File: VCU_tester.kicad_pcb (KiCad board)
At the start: 2 copper layers, 54.6 x 86.4 mm, 2 parts, among them P8 BeagleBone_Black_Header, P9 BeagleBone_Black_Header

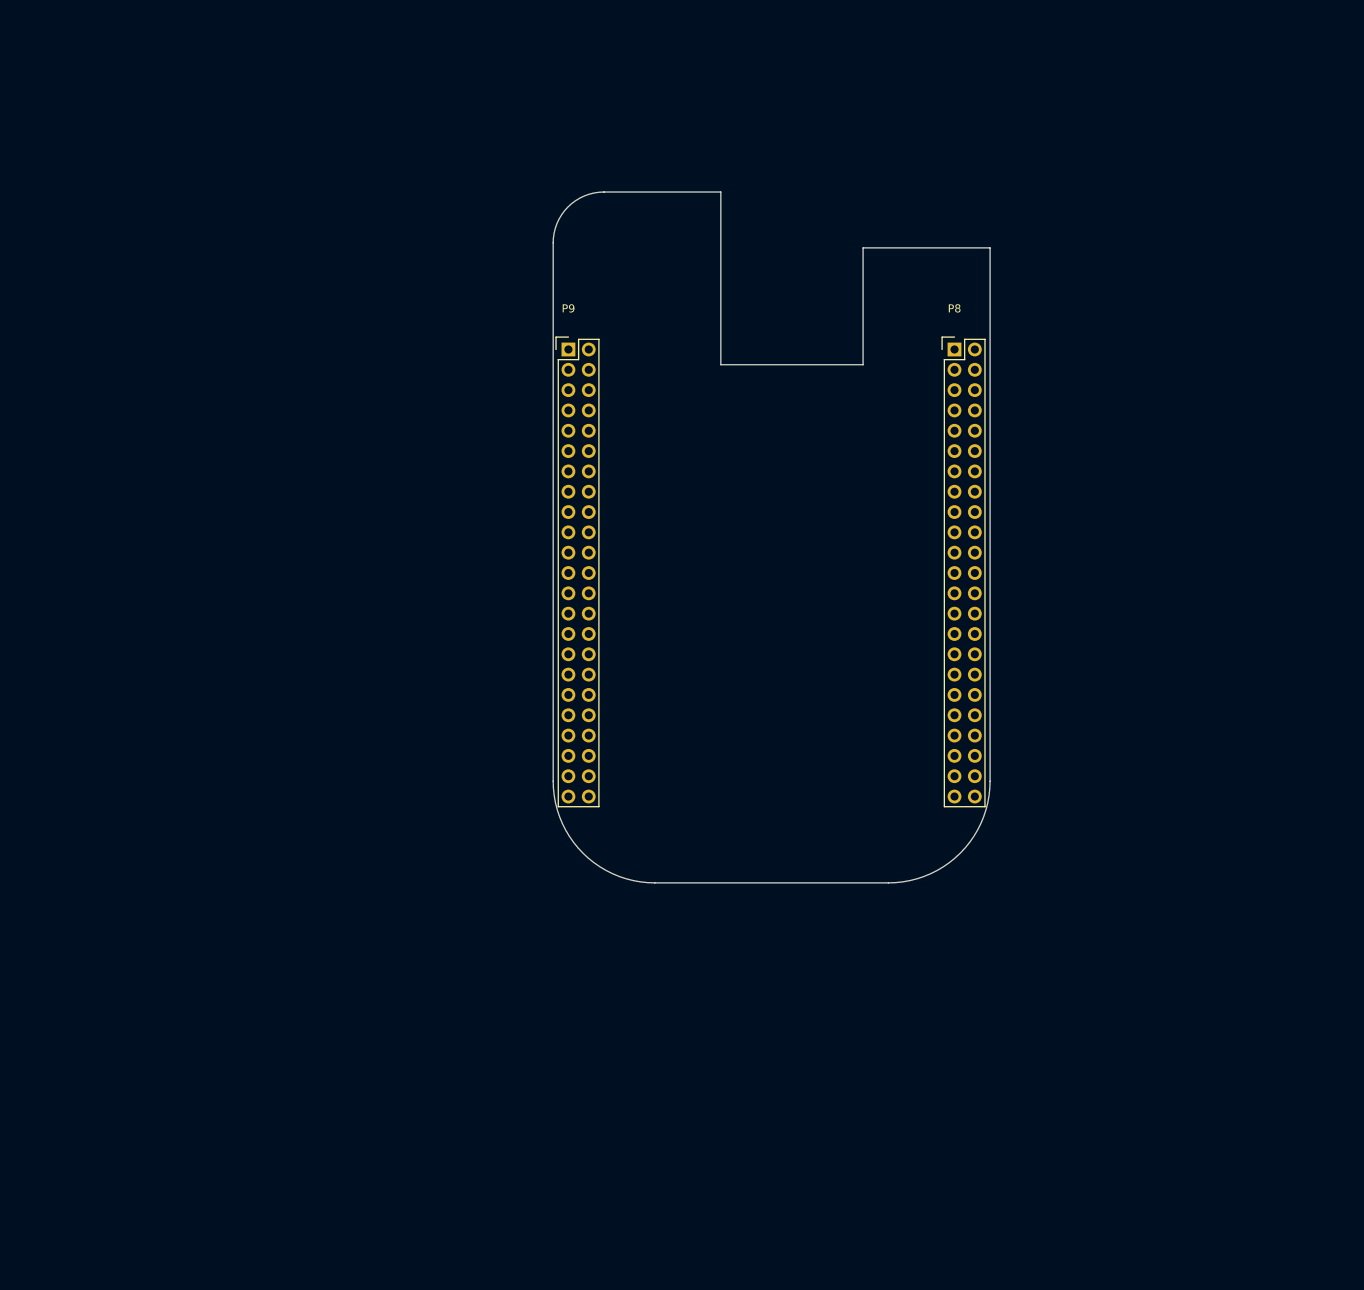
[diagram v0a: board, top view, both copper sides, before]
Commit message: parts assigned, layout started, CAN and RS232 sides done
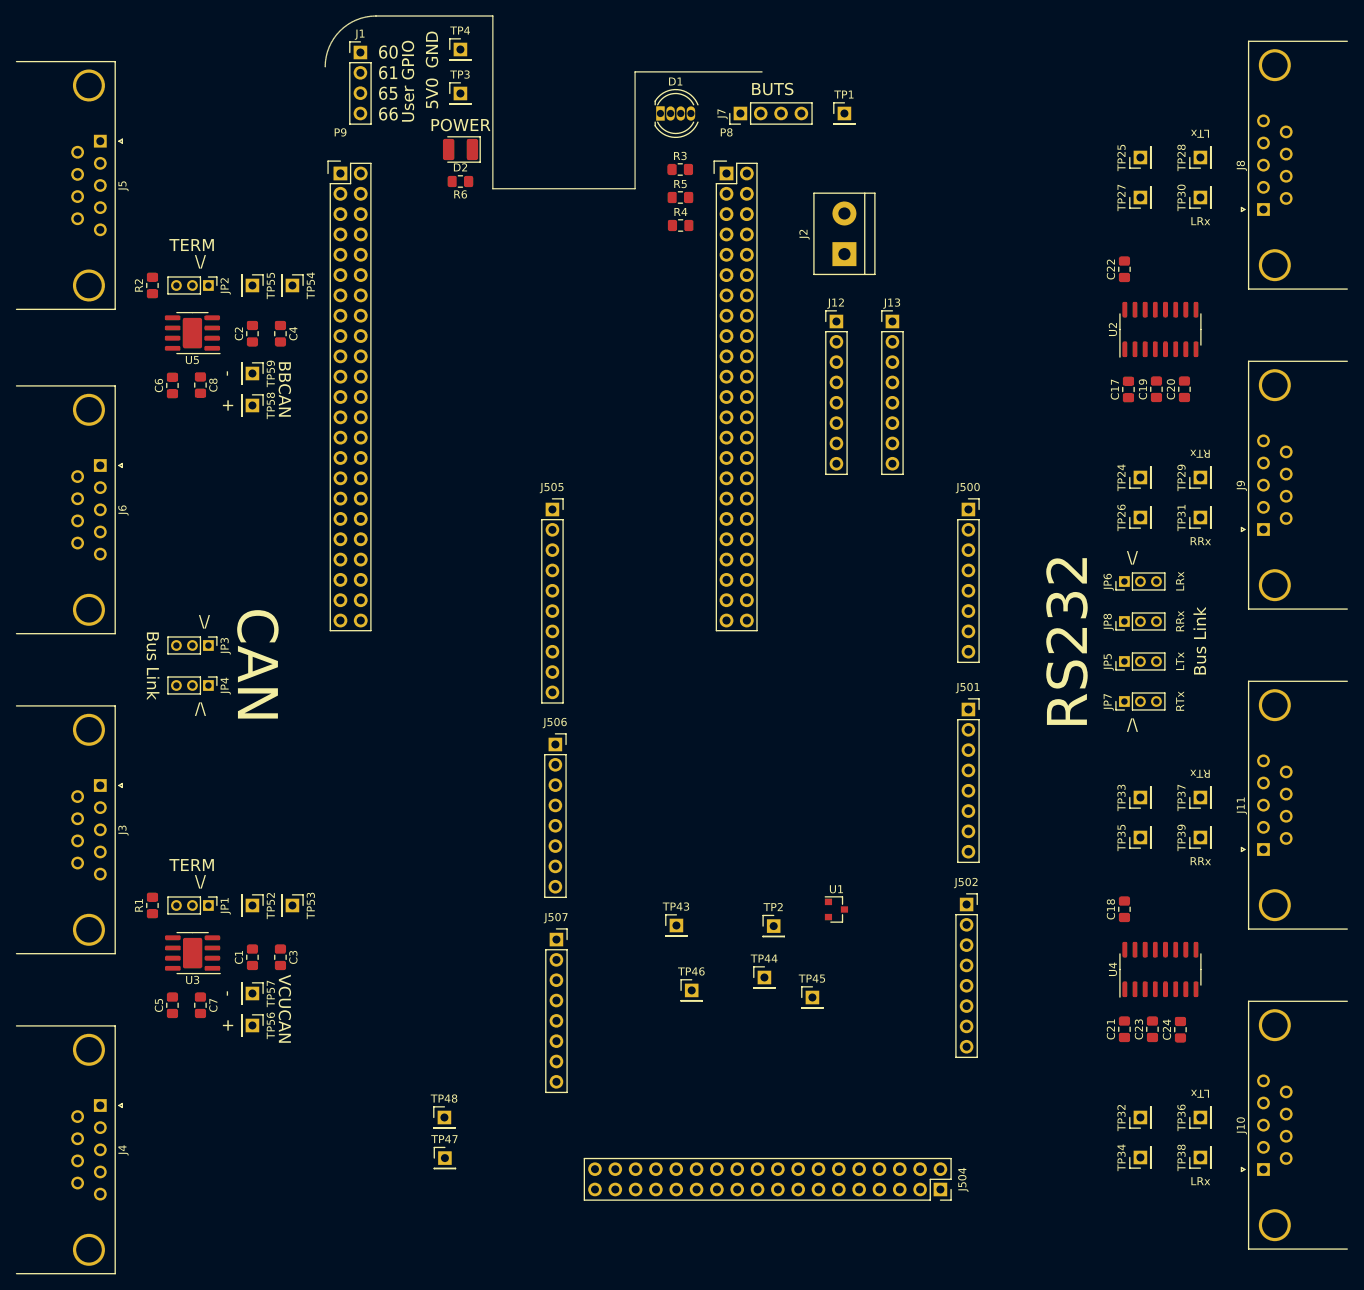
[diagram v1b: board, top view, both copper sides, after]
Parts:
- added C1: 10u, Capacitor_SMD:C_0805_2012Metric_Pad1.15x1.40mm_HandSolder, F.Cu at (76.9, 138.4)
- added C17: 100n, Capacitor_SMD:C_0805_2012Metric_Pad1.15x1.40mm_HandSolder, F.Cu at (186.4, 67.4)
- added C18: 100n, Capacitor_SMD:C_0805_2012Metric_Pad1.15x1.40mm_HandSolder, F.Cu at (185.9, 132.4)
- added C19: 100n, Capacitor_SMD:C_0805_2012Metric_Pad1.15x1.40mm_HandSolder, F.Cu at (189.9, 67.4)
- added C2: 10u, Capacitor_SMD:C_0805_2012Metric_Pad1.15x1.40mm_HandSolder, F.Cu at (76.9, 60.4)
- added C20: 100n, Capacitor_SMD:C_0805_2012Metric_Pad1.15x1.40mm_HandSolder, F.Cu at (193.4, 67.4)
- added C21: 100n, Capacitor_SMD:C_0805_2012Metric_Pad1.15x1.40mm_HandSolder, F.Cu at (185.9, 147.4)
- added C22: 100n, Capacitor_SMD:C_0805_2012Metric_Pad1.15x1.40mm_HandSolder, F.Cu at (185.9, 52.4)
- added C23: 100n, Capacitor_SMD:C_0805_2012Metric_Pad1.15x1.40mm_HandSolder, F.Cu at (189.4, 147.4)
- added C24: 100n, Capacitor_SMD:C_0805_2012Metric_Pad1.15x1.40mm_HandSolder, F.Cu at (192.9, 147.4)
- added C3: 100n, Capacitor_SMD:C_0805_2012Metric_Pad1.15x1.40mm_HandSolder, F.Cu at (80.4, 138.4)
- added C4: 100n, Capacitor_SMD:C_0805_2012Metric_Pad1.15x1.40mm_HandSolder, F.Cu at (80.4, 60.4)
- added C5: 10u, Capacitor_SMD:C_0805_2012Metric_Pad1.15x1.40mm_HandSolder, F.Cu at (66.9, 144.4)
- added C6: 10u, Capacitor_SMD:C_0805_2012Metric_Pad1.15x1.40mm_HandSolder, F.Cu at (66.9, 66.9)
- added C7: 100n, Capacitor_SMD:C_0805_2012Metric_Pad1.15x1.40mm_HandSolder, F.Cu at (70.4, 144.4)
- added C8: 100n, Capacitor_SMD:C_0805_2012Metric_Pad1.15x1.40mm_HandSolder, F.Cu at (70.4, 66.8)
- added D1: LED_RABG, LED_THT:LED_D5.0mm-4_RGB, F.Cu at (127.9, 32.9)
- added D2: LED, Diode_SMD:D_1210_3225Metric_Pad1.42x2.65mm_HandSolder, F.Cu at (102.9, 37.4)
- added J1: Conn_01x04_Male, Connector_PinHeader_2.54mm:PinHeader_1x04_P2.54mm_Vertical, F.Cu at (90.4, 25.3)
- added J10: DB9_Male, Connector_Dsub:DSUB-9_Male_Horizontal_P2.77x2.84mm_EdgePinOffset7.70mm_Housed_MountingHolesOffset9.12mm, F.Cu at (203.2, 164.9)
- added J11: DB9_Male, Connector_Dsub:DSUB-9_Male_Horizontal_P2.77x2.84mm_EdgePinOffset7.70mm_Housed_MountingHolesOffset9.12mm, F.Cu at (203.2, 124.9)
- added J12: Conn_01x08_Male, Connector_PinHeader_2.54mm:PinHeader_1x08_P2.54mm_Vertical, F.Cu at (149.9, 58.9)
- added J13: Conn_01x08_Male, Connector_PinHeader_2.54mm:PinHeader_1x08_P2.54mm_Vertical, F.Cu at (156.9, 58.9)
- added J2: Screw_Terminal_01x02, TerminalBlock:TerminalBlock_bornier-2_P5.08mm, F.Cu at (150.9, 50.5)
- added J3: DB9_Male, Connector_Dsub:DSUB-9_Male_Horizontal_P2.77x2.84mm_EdgePinOffset7.70mm_Housed_MountingHolesOffset9.12mm, F.Cu at (57.9, 116.9)
- added J4: DB9_Male, Connector_Dsub:DSUB-9_Male_Horizontal_P2.77x2.84mm_EdgePinOffset7.70mm_Housed_MountingHolesOffset9.12mm, F.Cu at (57.9, 156.9)
- added J5: DB9_Male, Connector_Dsub:DSUB-9_Male_Horizontal_P2.77x2.84mm_EdgePinOffset7.70mm_Housed_MountingHolesOffset9.12mm, F.Cu at (57.9, 36.3)
- added J500: Conn_01x08_Female, Connector_PinSocket_2.54mm:PinSocket_1x08_P2.54mm_Vertical, F.Cu at (166.4, 82.4)
- added J501: Conn_01x08_Female, Connector_PinSocket_2.54mm:PinSocket_1x08_P2.54mm_Vertical, F.Cu at (166.4, 107.4)
- added J502: Conn_01x08_Female, Connector_PinSocket_2.54mm:PinSocket_1x08_P2.54mm_Vertical, F.Cu at (166.1, 131.8)
- added J504: Conn_02x18_Odd_Even, Connector_PinSocket_2.54mm:PinSocket_2x18_P2.54mm_Vertical, F.Cu at (162.9, 167.4)
- added J505: Conn_01x10_Female, Connector_PinSocket_2.54mm:PinSocket_1x10_P2.54mm_Vertical, F.Cu at (114.4, 82.4)
- added J506: Conn_01x08_Female, Connector_PinSocket_2.54mm:PinSocket_1x08_P2.54mm_Vertical, F.Cu at (114.7, 111.8)
- added J507: Conn_01x08_Female, Connector_PinSocket_2.54mm:PinSocket_1x08_P2.54mm_Vertical, F.Cu at (114.9, 136.1)
- added J6: DB9_Male, Connector_Dsub:DSUB-9_Male_Horizontal_P2.77x2.84mm_EdgePinOffset7.70mm_Housed_MountingHolesOffset9.12mm, F.Cu at (57.9, 76.9)
- added J7: Conn_01x04_Male, Connector_PinHeader_2.54mm:PinHeader_1x04_P2.54mm_Vertical, F.Cu at (137.9, 32.9)
- added J8: DB9_Male, Connector_Dsub:DSUB-9_Male_Horizontal_P2.77x2.84mm_EdgePinOffset7.70mm_Housed_MountingHolesOffset9.12mm, F.Cu at (203.2, 44.9)
- added J9: DB9_Male, Connector_Dsub:DSUB-9_Male_Horizontal_P2.77x2.84mm_EdgePinOffset7.70mm_Housed_MountingHolesOffset9.12mm, F.Cu at (203.2, 84.9)
- added JP1: Jumper, Connector_PinHeader_2.00mm:PinHeader_1x03_P2.00mm_Vertical, F.Cu at (71.4, 131.9)
- added JP2: Jumper, Connector_PinHeader_2.00mm:PinHeader_1x03_P2.00mm_Vertical, F.Cu at (71.4, 54.4)
- added JP3: Jumper, Connector_PinHeader_2.00mm:PinHeader_1x03_P2.00mm_Vertical, F.Cu at (71.4, 99.4)
- added JP4: Jumper, Connector_PinHeader_2.00mm:PinHeader_1x03_P2.00mm_Vertical, F.Cu at (71.4, 104.4)
- added JP5: Jumper, Connector_PinHeader_2.00mm:PinHeader_1x03_P2.00mm_Vertical, F.Cu at (185.9, 101.4)
- added JP6: Jumper, Connector_PinHeader_2.00mm:PinHeader_1x03_P2.00mm_Vertical, F.Cu at (185.9, 91.4)
- added JP7: Jumper, Connector_PinHeader_2.00mm:PinHeader_1x03_P2.00mm_Vertical, F.Cu at (185.9, 106.4)
- added JP8: Jumper, Connector_PinHeader_2.00mm:PinHeader_1x03_P2.00mm_Vertical, F.Cu at (185.9, 96.4)
- added R1: 120R, Resistor_SMD:R_0805_2012Metric_Pad1.15x1.40mm_HandSolder, F.Cu at (64.4, 131.9)
- added R2: 120R, Resistor_SMD:R_0805_2012Metric_Pad1.15x1.40mm_HandSolder, F.Cu at (64.4, 54.4)
- added R3: 47R, Resistor_SMD:R_0805_2012Metric_Pad1.15x1.40mm_HandSolder, F.Cu at (130.3, 39.9)
- added R4: 20R, Resistor_SMD:R_0805_2012Metric_Pad1.15x1.40mm_HandSolder, F.Cu at (130.4, 46.9)
- added R5: 20R, Resistor_SMD:R_0805_2012Metric_Pad1.15x1.40mm_HandSolder, F.Cu at (130.4, 43.4)
- added R6: 100R, Resistor_SMD:R_0805_2012Metric_Pad1.15x1.40mm_HandSolder, F.Cu at (102.9, 41.4)
- added TP1: TestPoint, Connector_PinHeader_2.54mm:PinHeader_1x01_P2.54mm_Vertical, F.Cu at (150.9, 32.9)
- added TP2: TestPoint, Connector_PinHeader_2.54mm:PinHeader_1x01_P2.54mm_Vertical, F.Cu at (142.0, 134.5)
- added TP24: TestPoint, Connector_PinHeader_2.54mm:PinHeader_1x01_P2.54mm_Vertical, F.Cu at (187.9, 78.4)
- added TP25: TestPoint, Connector_PinHeader_2.54mm:PinHeader_1x01_P2.54mm_Vertical, F.Cu at (187.9, 38.4)
- added TP26: TestPoint, Connector_PinHeader_2.54mm:PinHeader_1x01_P2.54mm_Vertical, F.Cu at (187.9, 83.4)
- added TP27: TestPoint, Connector_PinHeader_2.54mm:PinHeader_1x01_P2.54mm_Vertical, F.Cu at (187.9, 43.4)
- added TP28: TestPoint, Connector_PinHeader_2.54mm:PinHeader_1x01_P2.54mm_Vertical, F.Cu at (195.4, 38.4)
- added TP29: TestPoint, Connector_PinHeader_2.54mm:PinHeader_1x01_P2.54mm_Vertical, F.Cu at (195.4, 78.4)
- added TP3: TestPoint, Connector_PinHeader_2.54mm:PinHeader_1x01_P2.54mm_Vertical, F.Cu at (102.9, 30.4)
- added TP30: TestPoint, Connector_PinHeader_2.54mm:PinHeader_1x01_P2.54mm_Vertical, F.Cu at (195.4, 43.4)
- added TP31: TestPoint, Connector_PinHeader_2.54mm:PinHeader_1x01_P2.54mm_Vertical, F.Cu at (195.4, 83.4)
- added TP32: TestPoint, Connector_PinHeader_2.54mm:PinHeader_1x01_P2.54mm_Vertical, F.Cu at (187.9, 158.4)
- added TP33: TestPoint, Connector_PinHeader_2.54mm:PinHeader_1x01_P2.54mm_Vertical, F.Cu at (187.9, 118.4)
- added TP34: TestPoint, Connector_PinHeader_2.54mm:PinHeader_1x01_P2.54mm_Vertical, F.Cu at (187.9, 163.4)
- added TP35: TestPoint, Connector_PinHeader_2.54mm:PinHeader_1x01_P2.54mm_Vertical, F.Cu at (187.9, 123.4)
- added TP36: TestPoint, Connector_PinHeader_2.54mm:PinHeader_1x01_P2.54mm_Vertical, F.Cu at (195.4, 158.4)
- added TP37: TestPoint, Connector_PinHeader_2.54mm:PinHeader_1x01_P2.54mm_Vertical, F.Cu at (195.4, 118.4)
- added TP38: TestPoint, Connector_PinHeader_2.54mm:PinHeader_1x01_P2.54mm_Vertical, F.Cu at (195.4, 163.4)
- added TP39: TestPoint, Connector_PinHeader_2.54mm:PinHeader_1x01_P2.54mm_Vertical, F.Cu at (195.4, 123.4)
- added TP4: TestPoint, Connector_PinHeader_2.54mm:PinHeader_1x01_P2.54mm_Vertical, F.Cu at (102.9, 24.9)
- added TP43: TestPoint, Connector_PinHeader_2.54mm:PinHeader_1x01_P2.54mm_Vertical, F.Cu at (129.9, 134.4)
- added TP44: TestPoint, Connector_PinHeader_2.54mm:PinHeader_1x01_P2.54mm_Vertical, F.Cu at (140.9, 140.9)
- added TP45: TestPoint, Connector_PinHeader_2.54mm:PinHeader_1x01_P2.54mm_Vertical, F.Cu at (146.9, 143.4)
- added TP46: TestPoint, Connector_PinHeader_2.54mm:PinHeader_1x01_P2.54mm_Vertical, F.Cu at (131.8, 142.5)
- added TP47: TestPoint, Connector_PinHeader_2.54mm:PinHeader_1x01_P2.54mm_Vertical, F.Cu at (100.9, 163.5)
- added TP48: TestPoint, Connector_PinHeader_2.54mm:PinHeader_1x01_P2.54mm_Vertical, F.Cu at (100.9, 158.4)
- added TP52: TestPoint, Connector_PinHeader_2.54mm:PinHeader_1x01_P2.54mm_Vertical, F.Cu at (76.9, 131.9)
- added TP53: TestPoint, Connector_PinHeader_2.54mm:PinHeader_1x01_P2.54mm_Vertical, F.Cu at (81.9, 131.9)
- added TP54: TestPoint, Connector_PinHeader_2.54mm:PinHeader_1x01_P2.54mm_Vertical, F.Cu at (81.9, 54.4)
- added TP55: TestPoint, Connector_PinHeader_2.54mm:PinHeader_1x01_P2.54mm_Vertical, F.Cu at (76.9, 54.4)
- added TP56: TestPoint, Connector_PinHeader_2.54mm:PinHeader_1x01_P2.54mm_Vertical, F.Cu at (76.9, 146.9)
- added TP57: TestPoint, Connector_PinHeader_2.54mm:PinHeader_1x01_P2.54mm_Vertical, F.Cu at (76.9, 142.9)
- added TP58: TestPoint, Connector_PinHeader_2.54mm:PinHeader_1x01_P2.54mm_Vertical, F.Cu at (76.9, 69.4)
- added TP59: TestPoint, Connector_PinHeader_2.54mm:PinHeader_1x01_P2.54mm_Vertical, F.Cu at (76.9, 65.4)
- added U1: REF3020, Package_TO_SOT_SMD:SOT-23, F.Cu at (149.9, 132.4)
- added U2: MAX3232, Package_SO:SOIC-16_3.9x9.9mm_P1.27mm, F.Cu at (190.4, 59.9)
- added U3: TCAN1042HVD, Package_SO:SOIC-8-1EP_3.9x4.9mm_P1.27mm_EP2.41x3.81mm, F.Cu at (69.4, 137.8)
- added U4: MAX3232, Package_SO:SOIC-16_3.9x9.9mm_P1.27mm, F.Cu at (190.4, 139.9)
- added U5: TCAN1042HVD, Package_SO:SOIC-8-1EP_3.9x4.9mm_P1.27mm_EP2.41x3.81mm, F.Cu at (69.4, 60.3)
- moved P8 36.0 mm to (136.1, 40.4)
- moved P9 36.0 mm to (87.9, 40.4)
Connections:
- net /ECAPWMO renamed /UART3_TXD
- net /ETHRPWM2B renamed /GPIO_23
- net /I2C2_SCL renamed /UART1_RTSN
- net /I2C_SDA renamed /UART1_CTSN
- net /LCD_AC_BIAS renamed /GPIO_89
- net /LCD_DATA0 renamed /GPIO_70
- net /LCD_DATA1 renamed /GPIO_71
- net /LCD_DATA10 renamed /UART3_CTSN
- net /LCD_DATA11 renamed /UART3_RTSN
- net /LCD_DATA12 renamed /UART4_CTSN
- net /LCD_DATA13 renamed /UART4_RSTN
- net /LCD_DATA14 renamed /UART5_CSTN+
- net /LCD_DATA15 renamed /UART5_RTSN
- net /LCD_DATA2 renamed /GPIO_72
- net /LCD_DATA3 renamed /GPIO_73
- net /LCD_DATA4 renamed /GPIO_74
- net /LCD_DATA5 renamed /GPIO_75
- net /LCD_DATA6 renamed /GPIO_76
- net /LCD_DATA7 renamed /GPIO_77
- net /LCD_DATA8 renamed /UART5_TXD+
- net /LCD_DATA9 renamed /UART5_RXD+
- net /LCD_HSYNC renamed /GPIO_87
- net /LCD_PCLK renamed /GPIO_88
- net /LCD_VSYNC renamed /GPIO_86
- net /MMC1_CLK renamed /GPIO_62
- net /MMC1_CMD renamed /GPIO_63
- net /MMC1_DAT1 renamed /GPIO_33
- net /MMC1_DAT2 renamed /MMC1_Dat2
- net /MMC1_DAT3 renamed /MMC1_dat3
- net /MMC1_DAT4 renamed /GPIO_36
- net /MMC1_DAT5 renamed /GPIO_37
- net /MMC1_DAT6 renamed /MMC1_Dat6
- net /MMC1_DAT7 renamed /MMC1_dat7
- net /MMC1_DATO renamed /GPIO_32
- net /SP11_CSO renamed /SPI1_CSO
- net /SP11_DO renamed /SPI1_DO
- net /SP11_SCLK renamed /SPI1_SCLK
- P8 pad 19: /ETHRPWM2A -> /GPIO_22
- P9 pad 14: /ETHRPWM1A -> /GPIO_50
- P9 pad 16: /ETHRPWM1B -> /GPIO_51
- P9 pad 17: /SPIO_CSO -> /DCAN0_RX
- P9 pad 18: /SPIO_D1 -> /DCAN0_TX
- P9 pad 21: /SPIO_DO -> /UART2_TXD
- P9 pad 22: /SPIO_SCLK -> /UART2_RXD
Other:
- board size 54.6 x 86.4 mm -> 54.6 x 21.6 mm
- board text added: "+"
- board text added: "-"
- board text added: "5V0"
- board text added: "60 61 65 66"
- board text added: "BBCAN"
- board text added: "BUTS"
- board text added: "Beagle side"
- board text added: "Bus Link"
- board text added: "CAN"
- board text added: "GND"
- board text added: "LRx"
- board text added: "LTx"
- board text added: "POWER"
- board text added: "RRx"
- board text added: "RS232"
- board text added: "RTx"
- board text added: "TERM"
- board text added: "User GPIO"
- board text added: "VCU side"
- board text added: "VCUCAN"
- board text added: "\/"
